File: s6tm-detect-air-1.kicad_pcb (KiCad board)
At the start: 2 copper layers, 71 parts, among them J1 Conn_01x04, J2 TC2030, J3 Conn_01x04, J4 Conn_01x04, J5 Conn_01x04_Pin, SW1 SW_Push, SW2 SW_Push, U1 SYS1002-H2, U10 004-1-0100, U2 MiCS-5524, U3 LMC6482, U4 HT753-1, U5 SN65HVD230, U6 STM32F103C8Tx, U7 HTU21, U8 LM73100, U9 ENS16x, Y1 8M

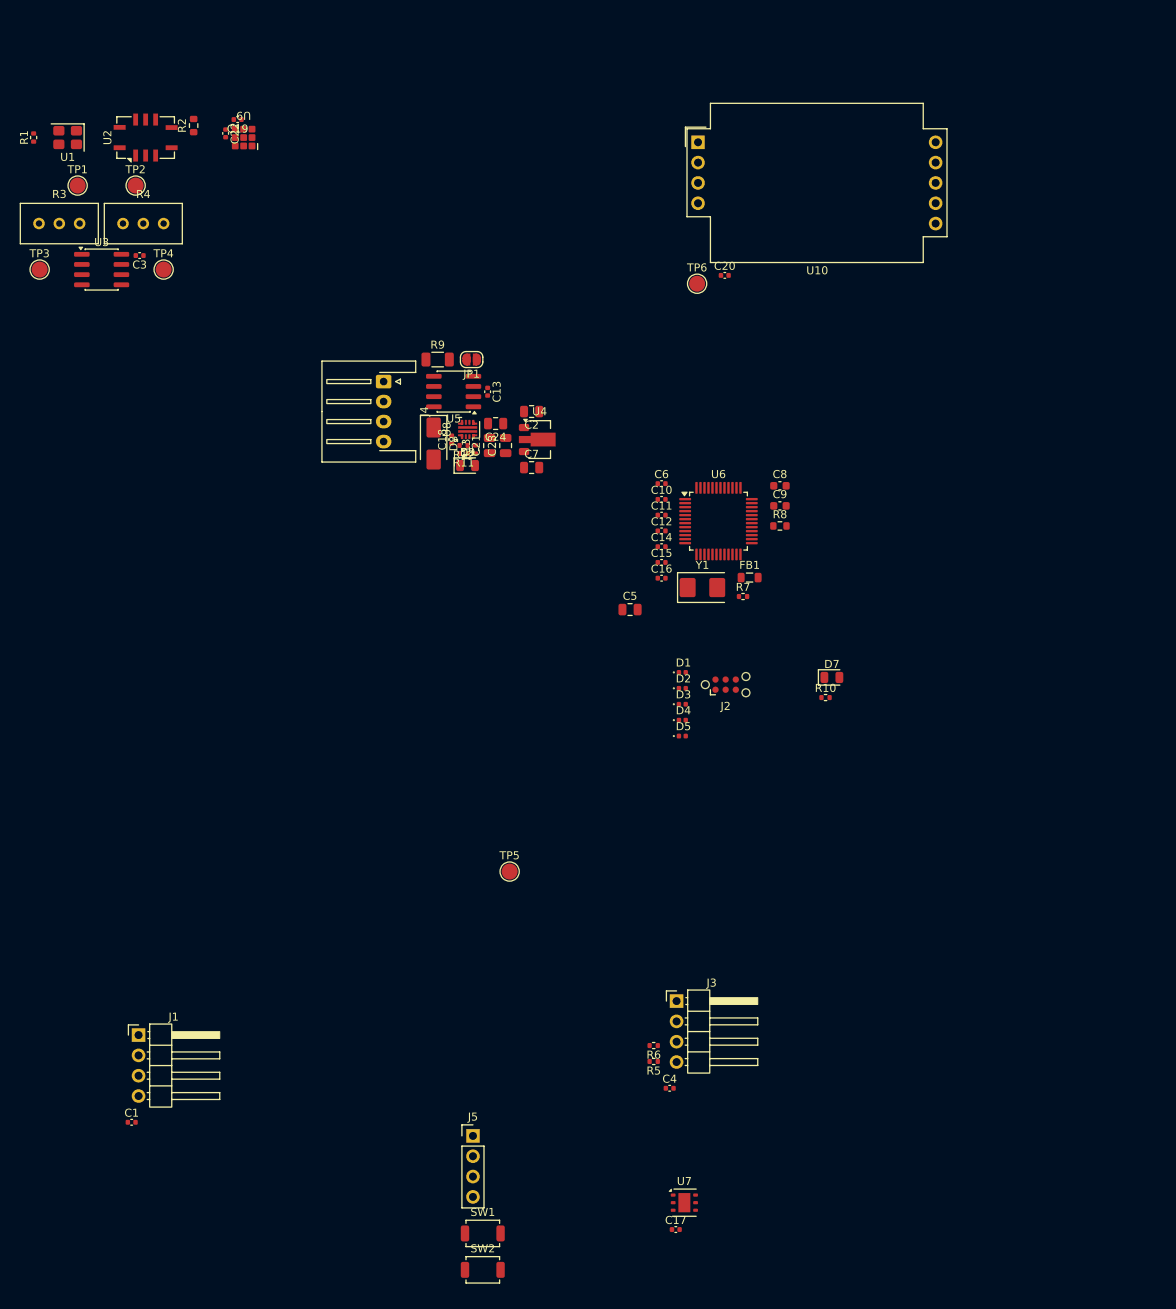
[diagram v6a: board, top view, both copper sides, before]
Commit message: pcb: add swd layout
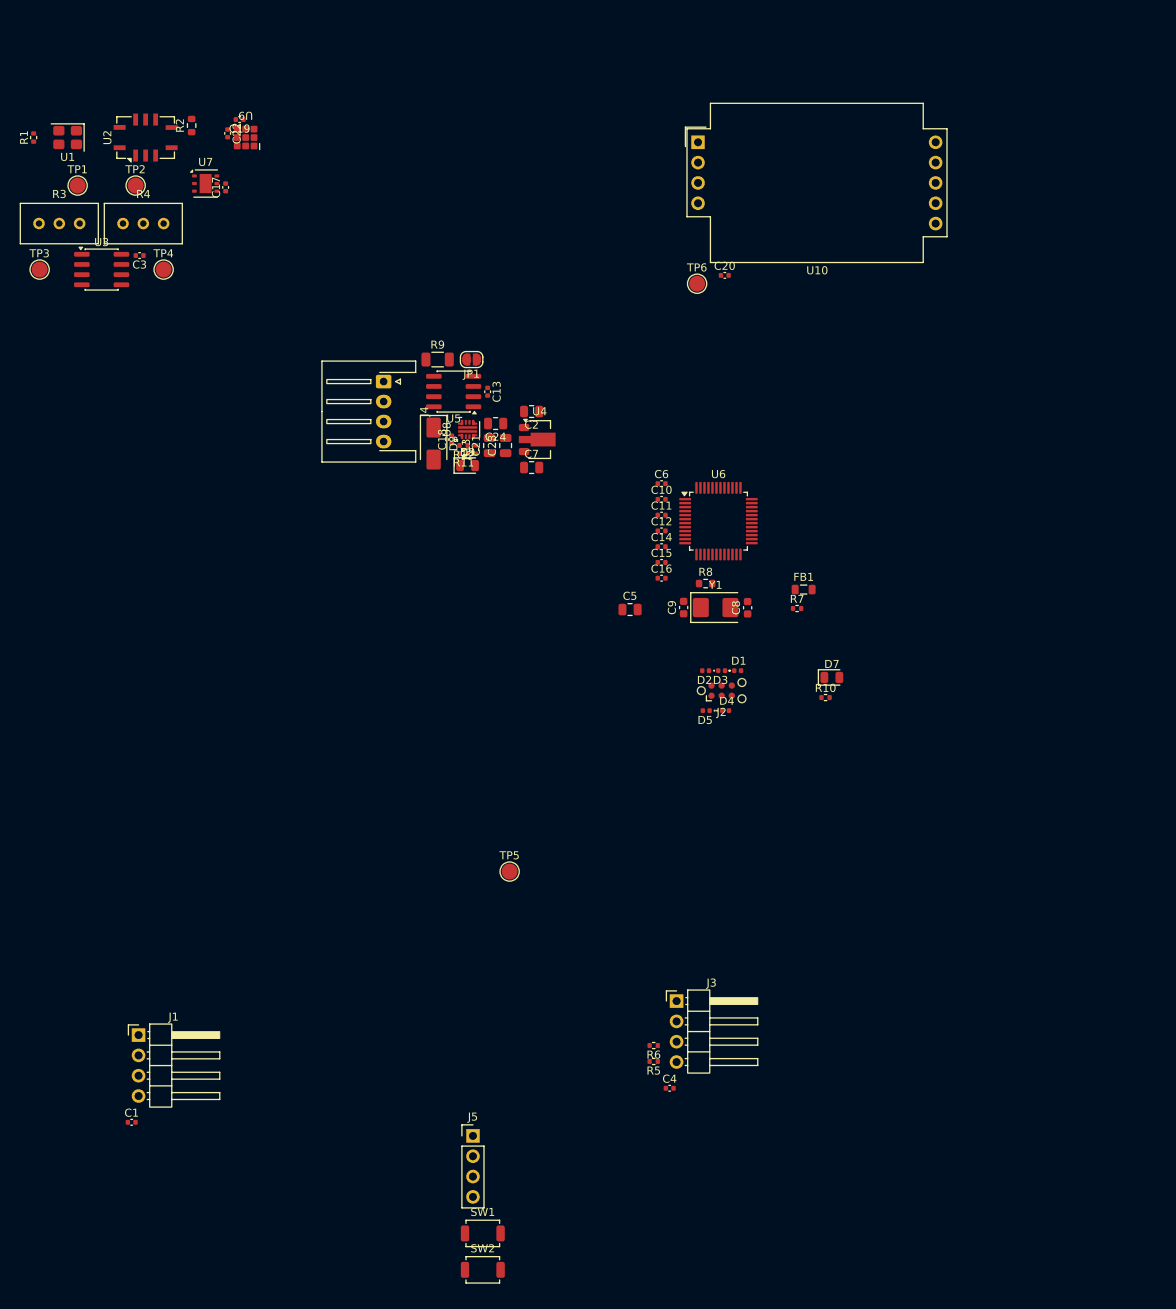
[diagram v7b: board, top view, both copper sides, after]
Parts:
- moved C17 141.9 mm to (48.2, 45.7), turned to 90 degrees
- moved U7 140.7 mm to (45.8, 45.2)
- moved C9 17.5 mm to (105.5, 98.2), turned to 90 degrees
- moved C8 15.8 mm to (113.5, 98.3), turned to 90 degrees
- moved R8 11.7 mm to (108.2, 95.2)
- moved R7 6.92 mm to (119.7, 98.4)
- moved FB1 6.92 mm to (120.5, 96.0)
- moved D1 6.92 mm to (112.2, 106.1)
- moved D3 6.47 mm to (110.2, 106.1), turned to 180 degrees
- moved D4 5.54 mm to (110.8, 111.1)
- moved D5 4.36 mm to (108.3, 111.1), turned to 180 degrees
- moved D2 3.66 mm to (108.2, 106.1), turned to 180 degrees
- moved Y1 3.00 mm to (109.5, 98.2)
- moved J2 0.90 mm to (110.2, 108.6)
- moved C19 0.25 mm to (50.0, 37.2)
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
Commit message: pcb: add module layout
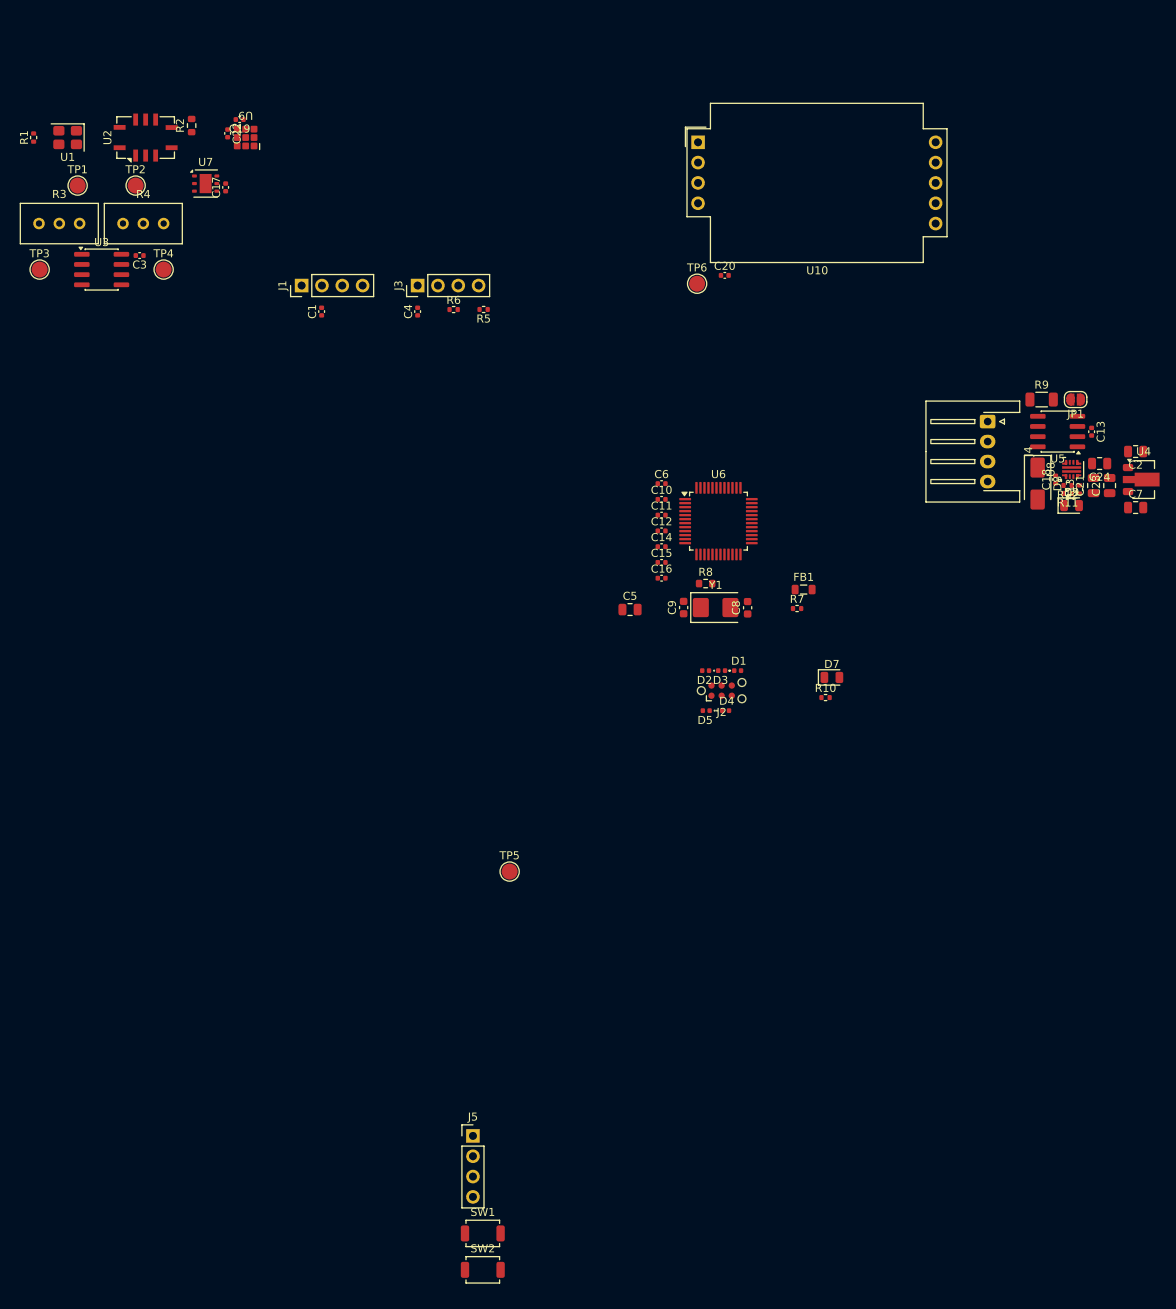
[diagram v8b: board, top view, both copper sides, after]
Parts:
- J1, J3: footprint Connector_PinHeader_2.54mm:PinHeader_1x04_P2.54mm_Horizontal -> Connector_PinHeader_2.54mm:PinHeader_1x04_P2.54mm_Vertical
- moved C1 104.1 mm to (60.2, 61.2), turned to 90 degrees
- moved C4 102.1 mm to (72.2, 61.2), turned to 90 degrees
- moved R5 96.4 mm to (80.5, 61.0)
- moved J1 95.9 mm to (57.8, 58.0), turned to 90 degrees
- moved R6 95.3 mm to (76.8, 61.0), turned to 0 degrees
- moved J3 95.1 mm to (72.2, 58.0), turned to 90 degrees
- moved C21 75.7 mm to (156.7, 83.0)
- moved D9 75.7 mm to (154.0, 85.5)
- moved R13 75.7 mm to (155.0, 83.5)
- moved C13 75.7 mm to (156.5, 76.3)
- moved C18 75.7 mm to (152.0, 82.2)
- moved C2 75.7 mm to (162.0, 78.8)
- moved C23 75.7 mm to (158.8, 83.0)
- moved C24 75.7 mm to (157.5, 80.2)
- moved C7 75.7 mm to (162.0, 85.8)
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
